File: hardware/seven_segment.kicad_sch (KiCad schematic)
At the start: 50 parts, among them J1 Conn_02x08_Odd_Even, J2 PJ-102AH, J3 7761, J4 7761, J5 Conn_01x02, SW1 SW_Push, SW2 SW_Push, SW3 SW_Push, SW4 SW_Push, U1 STM32F051K8Ux, U10 TPS22810DRV, U11 TPS22810DRV, U12 TPS22810DRV, U13 TPS22810DRV, U2 ULN2003A, U3 ULN2003A, U4 AP1117-33, U5 TPS22810DRV, U6 74HC238, U7 TPS22810DRV, U8 TPS22810DRV, U9 TPS22810DRV

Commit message: hardware: Start work on version 2
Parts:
- removed C4: C, Resistor_SMD:R_0603_1608Metric, symbol Device:C
- removed DISP1, DISP2, DISP3, DISP4, DISP5, DISP6, DISP7, DISP8: Conn_01x01, klauke:2025, symbol Connector_Generic:Conn_01x01
- removed J1: Conn_02x08_Odd_Even, Connector_PinHeader_2.54mm:PinHeader_2x08_P2.54mm_Horizontal, symbol Connector_Generic:Conn_02x08_Odd_Even
- removed J3, J4: 7761, 7761:KEYSTONE_7761, symbol 7761:7761
- removed J5: Conn_01x02, Connector_PinHeader_2.54mm:PinHeader_1x02_P2.54mm_Vertical, symbol Connector_Generic:Conn_01x02
- removed R7, R8: R, Resistor_SMD:R_0603_1608Metric, symbol Device:R
- removed SW4: SW_Push, pushbutton:TO_6083716_WRE, symbol Switch:SW_Push
- removed U10, U11, U12, U13, U5, U7, U8, U9: TPS22810DRV, Package_SON:WSON-6-1EP_2x2mm_P0.65mm_EP1x1.6mm, symbol Power_Management:TPS22810DRV
- removed U6: 74HC238, Package_SO:SOIC-16W_5.3x10.2mm_P1.27mm, symbol 74xx_IEEE:74HC238
- added BOOT0: BOOT0, TestPoint:TestPoint_Pad_D1.5mm, symbol Connector:TestPoint
- added J1: Conn_01x16, Connector_PinHeader_2.54mm:PinHeader_2x08_P2.54mm_Horizontal, symbol Connector_Generic:Conn_01x16
- added J3: Conn_01x04, Connector_JST:JST_EH_B4B-EH-A_1x04_P2.50mm_Vertical, symbol Connector_Generic:Conn_01x04
- added U10, U7, U8, U9: TPS22810DBVT, Package_TO_SOT_SMD:SOT-23-6, symbol TPS22810DBVT:TPS22810DBVT
- added U11: STM32F051C8Tx, Package_QFP:LQFP-48_7x7mm_P0.5mm, symbol MCU_ST_STM32F0:STM32F051C8Tx
- added U12: STM32F051C8Ux, Package_DFN_QFN:QFN-48-1EP_7x7mm_P0.5mm_EP5.6x5.6mm, symbol MCU_ST_STM32F0:STM32F051C8Ux
- added U5, U6: 74HC595, Package_SO:SOP-16_4.55x10.3mm_P1.27mm, symbol 74xx:74HC595
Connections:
- net sel_en is gone; now on net SWCLK: U1.25 (PA15)
- net +12V: now also U10.1 (VIN), U7.1 (VIN), U8.1 (VIN), U9.1 (VIN)
- net +3V3: now also U5.10 (~{SRCLR}), U5.16 (VCC), U6.10 (~{SRCLR}), U6.16 (VCC); no longer R9.2
- net GND: now also R9.1, U10.2 (GND), U5.8 (GND), U6.8 (GND), U7.2 (GND), U8.2 (GND), U9.2 (GND)
- net SWCLK: now also SWD1.3 (Pin_3); no longer SWD1.4 (Pin_4), U1.24 (PA14)
- net SWDIO: now also SWD1.4 (Pin_4), U1.24 (PA14); no longer SWD1.3 (Pin_3), U1.23 (PA13)
- net at U3.10 (O7): now also J1.16 (Pin_16)
- net at U3.11 (O6): now also J1.15 (Pin_15)
- net at U3.12 (O5): now also J1.14 (Pin_14)
- net at U3.13 (O4): now also J1.13 (Pin_13)
- net at U3.14 (O3): now also J1.12 (Pin_12)
- net at U3.15 (O2): now also J1.11 (Pin_11)
- net at U3.16 (O1): now also J1.10 (Pin_10)
- net at U2.10 (O7): now also J1.9 (Pin_9)
- net at U2.11 (O6): now also J1.8 (Pin_8)
- net at U2.12 (O5): now also J1.7 (Pin_7)
- net at U2.13 (O4): now also J1.6 (Pin_6)
- net at U2.14 (O3): now also J1.5 (Pin_5)
- net at U2.15 (O2): now also J1.4 (Pin_4)
- net at U2.16 (O1): now also J1.3 (Pin_3)
- net at U1.31 (BOOT0): now also R9.2, BOOT0.1; no longer R9.1
- net clrA: no longer names the net of U3.7 (I7)
- net clrA: now also U6.7 (QH); no longer U1.13 (PA7)
- net clrB: no longer names the net of U3.6 (I6)
- net clrB: now also U6.6 (QG); no longer U1.14 (PB0)
- net clrC: no longer names the net of U3.5 (I5)
- net clrC: now also U6.5 (QF); no longer U1.15 (PB1)
- net clrD: no longer names the net of U3.4 (I4)
- net clrD: now also U6.4 (QE); no longer U1.16 (PB2)
- net clrE: no longer names the net of U1.18 (PA8)
- net clrE: now also U5.13 (~{OE}), U6.13 (~{OE}); no longer U3.3 (I3)
- net clrF: no longer names the net of U3.2 (I2)
- net clrF: now also U6.2 (QC); no longer U1.21 (PA11)
- net clrG: no longer names the net of U3.1 (I1)
- net clrG: now also U6.1 (QB); no longer U1.22 (PA12)
- net sel0: no longer names the net of U1.28 (PB5)
- net sel1: no longer names the net of U1.27 (PB4)
- net sel2: no longer names the net of U1.26 (PB3)
- net setA: no longer names the net of U1.6 (PA0)
- net setA: now also U7.3 (EN/UVLO); no longer U2.7 (I7)
- net setB: no longer names the net of U1.7 (PA1)
- net setB: now also U8.3 (EN/UVLO); no longer U2.6 (I6)
- net setC: no longer names the net of U2.5 (I5)
- net setC: now also U5.5 (QF); no longer U1.8 (PA2)
- net setD: no longer names the net of U1.9 (PA3)
- net setD: now also U10.3 (EN/UVLO); no longer U2.4 (I4)
- net setE: no longer names the net of U2.3 (I3)
- net setE: now also U5.3 (QD); no longer U1.10 (PA4)
- net setF: no longer names the net of U2.2 (I2)
- net setF: now also U5.2 (QC); no longer U1.11 (PA5)
- net setG: no longer names the net of U2.1 (I1)
- net setG: now also U5.1 (QB); no longer U1.12 (PA6)
- new net: J3.2 (Pin_2), U8.6 (VOUT)
- new net: J3.4 (Pin_4), U10.6 (VOUT)
- new net: J3.1 (Pin_1), U7.6 (VOUT)
- new net: U2.4 (I4), U5.4 (QE)
- new net: U2.6 (I6), U5.6 (QG)
- new net: U2.7 (I7), U5.7 (QH)
- new net: U5.9 (QH'), U6.14 (SER)
- new net: J3.3 (Pin_3), U9.6 (VOUT)
- new net: U3.3 (I3), U6.3 (QD)
- new net: U1.8 (PA2), U9.3 (EN/UVLO)
- new net MISO: U1.12 (PA6)
- new net MOSI: U1.13 (PA7), U5.14 (SER)
- new net SCK: U1.11 (PA5), U5.11 (SRCLK), U5.12 (RCLK), U6.11 (SRCLK), U6.12 (RCLK)
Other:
- moved on the sheet: R9, SWD1, U1, U2, U3, UART1

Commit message: hardware: Version 2
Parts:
- removed C3: C, Resistor_SMD:R_0603_1608Metric, symbol Device:C
- removed SW3: SW_Push, pushbutton:TO_6083716_WRE, symbol Switch:SW_Push
- removed U11: STM32F051C8Tx, Package_QFP:LQFP-48_7x7mm_P0.5mm, symbol MCU_ST_STM32F0:STM32F051C8Tx
- removed U12: STM32F051C8Ux, Package_DFN_QFN:QFN-48-1EP_7x7mm_P0.5mm_EP5.6x5.6mm, symbol MCU_ST_STM32F0:STM32F051C8Ux
- added BT1: Battery_Cell, Battery:BatteryHolder_Keystone_3000_1x12mm, symbol Device:Battery_Cell
- added C10, C4: C, Resistor_SMD:R_0402_1005Metric_Pad0.72x0.64mm_HandSolder, symbol Device:C
- added D1: LED, Connector_PinHeader_2.54mm:PinHeader_1x02_P2.54mm_Vertical, symbol Device:LED
- added R7: 10k, Resistor_SMD:R_0603_1608Metric, symbol Device:R
- added U11: MCP7940N-xSN, Package_SO:SO-8_3.9x4.9mm_P1.27mm, symbol Timer_RTC:MCP7940N-xSN
- added Y1: Crystal, Crystal:Crystal_SMD_3215-2Pin_3.2x1.5mm, symbol Device:Crystal
- C5, C6: footprint Capacitor_THT:CP_Radial_D7.5mm_P2.50mm -> Capacitor_SMD:CP_Elec_6.3x5.9
- R3, R6, R9: value R -> 10k
- renumbered SW1 to RST1
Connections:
- net +3V3: now also R6.2, D1.2 (A), U11.8 (VCC)
- net GND: now also BT1.2 (-), C10.2, C4.2, U11.4 (VSS)
- net at U8.3 (EN/UVLO): now also U1.15 (PB1); no longer U1.7 (PA1)
- net SDA: now reaches R3.1
- net SDA: now also U1.30 (PB7), U11.5 (SDA); no longer R6.2
- net at U10.3 (EN/UVLO): now also U1.18 (PA8); no longer U1.9 (PA3)
- net at U7.3 (EN/UVLO): now also U1.14 (PB0); no longer U1.6 (PA0)
- net at U5.13 (~{OE}), U6.13 (~{OE}): now also U1.10 (PA4); no longer U1.18 (PA8)
- net at R5.1: now also U1.8 (PA2); no longer U1.29 (PB6)
- net at U9.3 (EN/UVLO): now also U1.16 (PB2); no longer U1.8 (PA2)
- net SCL: now reaches R6.1
- net SCL: now also U1.29 (PB6), U11.6 (SCL); no longer U1.30 (PB7)
- net at U1.28 (PB5): now also U11.7 (MFP)
- new net: C10.1, U11.1 (X1), Y1.2
- new net: C4.1, U11.2 (X2), Y1.1
- new net: BT1.1 (+), U11.3 (VBAT)
- new net: D1.1 (K), R7.2
- new net: R7.1, U1.9 (PA3)
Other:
- moved on the sheet: BOOT0, C1, C2, J3, R1, R2, R4, R5, R9, RST1, SW2, U10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

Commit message: hardware: revision 3
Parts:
- removed BOOT0: BOOT0, TestPoint:TestPoint_Pad_D1.5mm, symbol Connector:TestPoint
- removed BT1: Battery_Cell, Battery:BatteryHolder_Keystone_3000_1x12mm, symbol Device:Battery_Cell
- removed C10: C, Resistor_SMD:R_0402_1005Metric_Pad0.72x0.64mm_HandSolder, symbol Device:C
- removed C5, C6: C_Polarized, Capacitor_SMD:CP_Elec_6.3x5.9, symbol Device:C_Polarized
- removed D1: LED, Connector_PinHeader_2.54mm:PinHeader_1x02_P2.54mm_Vertical, symbol Device:LED
- removed SWD1, UART1: Conn_01x04, Connector_PinHeader_2.54mm:PinHeader_1x04_P2.54mm_Vertical, symbol Connector_Generic:Conn_01x04
- removed U1: STM32F051K8Ux, Package_DFN_QFN:QFN-32-1EP_5x5mm_P0.5mm_EP3.45x3.45mm, symbol MCU_ST_STM32F0:STM32F051K8Ux
- removed U10, U7, U8, U9: TPS22810DBVT, Package_TO_SOT_SMD:SOT-23-6, symbol TPS22810DBVT:TPS22810DBVT
- removed U11: MCP7940N-xSN, Package_SO:SO-8_3.9x4.9mm_P1.27mm, symbol Timer_RTC:MCP7940N-xSN
- removed U4: AP1117-33, Package_TO_SOT_SMD:SOT-223-3_TabPin2, symbol Regulator_Linear:AP1117-33
- removed Y1: Crystal, Crystal:Crystal_SMD_3215-2Pin_3.2x1.5mm, symbol Device:Crystal
- added C3: 10p, Resistor_SMD:R_0603_1608Metric, symbol Device:C
- added J5: Conn_01x06, Connector:Tag-Connect_TC2030-IDC-NL_2x03_P1.27mm_Vertical, symbol Connector_Generic:Conn_01x06
- added K1, K2, K3, K4: ~, 00_customfootprints:G6DN-1A-SL, symbol 00_customsymbols:Relay
- added L1: 2.2u, Inductor_SMD:L_Vishay_IHLP-1212, symbol Device:L
- added R10, R11: 10k, Resistor_SMD:R_0603_1608Metric, symbol Device:R
- added R8: R, Resistor_SMD:R_0603_1608Metric, symbol Device:R
- added U1: ESP32-WROOM-32E, RF_Module:ESP32-WROOM-32D, symbol RF_Module:ESP32-WROOM-32E
- added U4: TPS562200, Package_TO_SOT_SMD:SOT-23-6, symbol Regulator_Switching:TPS562200
- added U7: ULN2003A, Package_SO:SOP-16_3.9x9.9mm_P1.27mm, symbol Transistor_Array:ULN2003A
- C4: value C -> 0.1u; footprint Resistor_SMD:R_0402_1005Metric_Pad0.72x0.64mm_HandSolder -> Resistor_SMD:R_0603_1608Metric
- C7, C8: value C -> 22u; footprint Resistor_SMD:R_0805_2012Metric -> Capacitor_SMD:C_0805_2012Metric
- C9: value C -> 10u; footprint Resistor_SMD:R_0805_2012Metric -> Capacitor_SMD:C_0805_2012Metric
- J1: footprint Connector_PinHeader_2.54mm:PinHeader_2x08_P2.54mm_Horizontal -> Connector_PinHeader_2.54mm:PinHeader_2x08_P2.54mm_Vertical
- R1, R2: value R -> 10k
- R3, R6, R7: value 10k -> R
- R9: value 10k -> 33.2k
- U2, U3, U5, U6: footprint Package_SO:SOP-16_4.55x10.3mm_P1.27mm -> Package_SO:SOP-16_3.9x9.9mm_P1.27mm
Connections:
- net +12V: now also C9.1, R3.2, R6.2, R7.2, K1.3, K2.3, K3.3, K4.3, R11.1, R8.2, U4.3 (VIN), U7.9 (COM)
- net +3V3: now also R1.1, R2.1, R9.1, J5.2 (Pin_2), L1.2, U1.2 (VDD); no longer C9.1, R1.2, R2.2, R3.2, R6.2
- net GND: now also C3.2, J5.4 (Pin_4), R10.2, U1.1 (GND), U1.15 (GND), U1.38 (GND), U1.39 (GND), U4.1 (GND), U7.5 (I5), U7.6 (I6), U7.7 (I7), U7.8 (GND); no longer C4.2, R9.1
- net at C4.1: now also U4.6 (VBST)
- net at J3.2 (Pin_2): now also K2.4
- net at R9.2: now also R10.1, U4.4 (VFB)
- net at J3.4 (Pin_4): now also K4.4
- net at R4.1: now also C1.1, U1.31 (IO19)
- net at R4.2, RST1.1: no longer C1.1, R1.1
- net at J3.1 (Pin_1): now also K1.4
- net at U5.1 (QB): now also U2.7 (I7); no longer U2.1 (I1)
- net at U5.13 (~{OE}), U6.13 (~{OE}): now also U1.9 (IO33)
- net at U5.2 (QC): now also U2.6 (I6); no longer U2.2 (I2)
- net at U5.3 (QD): now also U2.5 (I5); no longer U2.3 (I3)
- net at U5.5 (QF): now also U2.3 (I3); no longer U2.5 (I5)
- net at U5.6 (QG): now also U2.2 (I2); no longer U2.6 (I6)
- net at U5.7 (QH): now also U2.1 (I1); no longer U2.7 (I7)
- net at J3.3 (Pin_3): now also K3.4
- net at U6.1 (QB): now also U3.7 (I7); no longer U3.1 (I1)
- net at U6.2 (QC): now also U3.6 (I6); no longer U3.2 (I2)
- net at U6.3 (QD): now also U3.5 (I5); no longer U3.3 (I3)
- net at U6.5 (QF): now also U3.3 (I3); no longer U3.5 (I5)
- net at U6.6 (QG): now also U3.2 (I2); no longer U3.6 (I6)
- net at U6.7 (QH): now also U3.1 (I1); no longer U3.7 (I7)
- net at J1.10 (Pin_10): now also U3.10 (O7); no longer U3.16 (O1)
- net at J1.11 (Pin_11): now also U3.11 (O6); no longer U3.15 (O2)
- net at J1.12 (Pin_12): now also U3.12 (O5); no longer U3.14 (O3)
- net at J1.14 (Pin_14): now also U3.14 (O3); no longer U3.12 (O5)
- net at J1.15 (Pin_15): now also U3.15 (O2); no longer U3.11 (O6)
- net at J1.16 (Pin_16): now also U3.16 (O1); no longer U3.10 (O7)
- net at J1.3 (Pin_3): now also U2.10 (O7); no longer U2.16 (O1)
- net at J1.4 (Pin_4): now also U2.11 (O6); no longer U2.15 (O2)
- net at J1.5 (Pin_5): now also U2.12 (O5); no longer U2.14 (O3)
- net at J1.7 (Pin_7): now also U2.14 (O3); no longer U2.12 (O5)
- net at J1.8 (Pin_8): now also U2.15 (O2); no longer U2.11 (O6)
- net at J1.9 (Pin_9): now also U2.16 (O1); no longer U2.10 (O7)
- net at R5.1: now also C2.1, U1.26 (IO4)
- net at R5.2, SW2.1: no longer C2.1, R2.1
- net at R7.1: now also K3.2
- net MOSI: no longer names the net of U5.14 (SER)
- net MOSI: now also U1.8 (IO32)
- net SCK: no longer names the net of U5.11 (SRCLK), U5.12 (RCLK), U6.11 (SRCLK), U6.12 (RCLK)
- net SCK: now also U1.10 (IO25)
- net SCL: no longer names the net of R6.1
- net SCL: now also K2.2
- net SDA: no longer names the net of R3.1
- net SDA: now also K1.2
- new net: K1.1, U7.15 (O2)
- new net: R11.2, U4.5 (EN)
- new net: C3.1, J5.1 (Pin_1), R2.2, U1.3 (EN)
- new net: J5.3 (Pin_3), U1.34 (RXD0/IO3)
- new net: J5.5 (Pin_5), U1.35 (TXD0/IO1)
- new net: J5.6 (Pin_6), U1.25 (IO0)
- new net: K3.1, U7.13 (O4)
- new net: R1.2, U1.27 (IO16)
- new net: C4.2, L1.1, U4.2 (SW)
- new net: K4.1, U7.14 (O3)
- new net: K4.2, R8.1
- new net: K2.1, U7.16 (O1)
- new net: U1.28 (IO17), U7.1 (I1)
- new net: U1.30 (IO18), U7.2 (I2)
- new net: U1.36 (IO22), U7.3 (I3)
- new net: U1.37 (IO23), U7.4 (I4)
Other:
- moved on the sheet: J2, J3, R4, R5, RST1, SW2

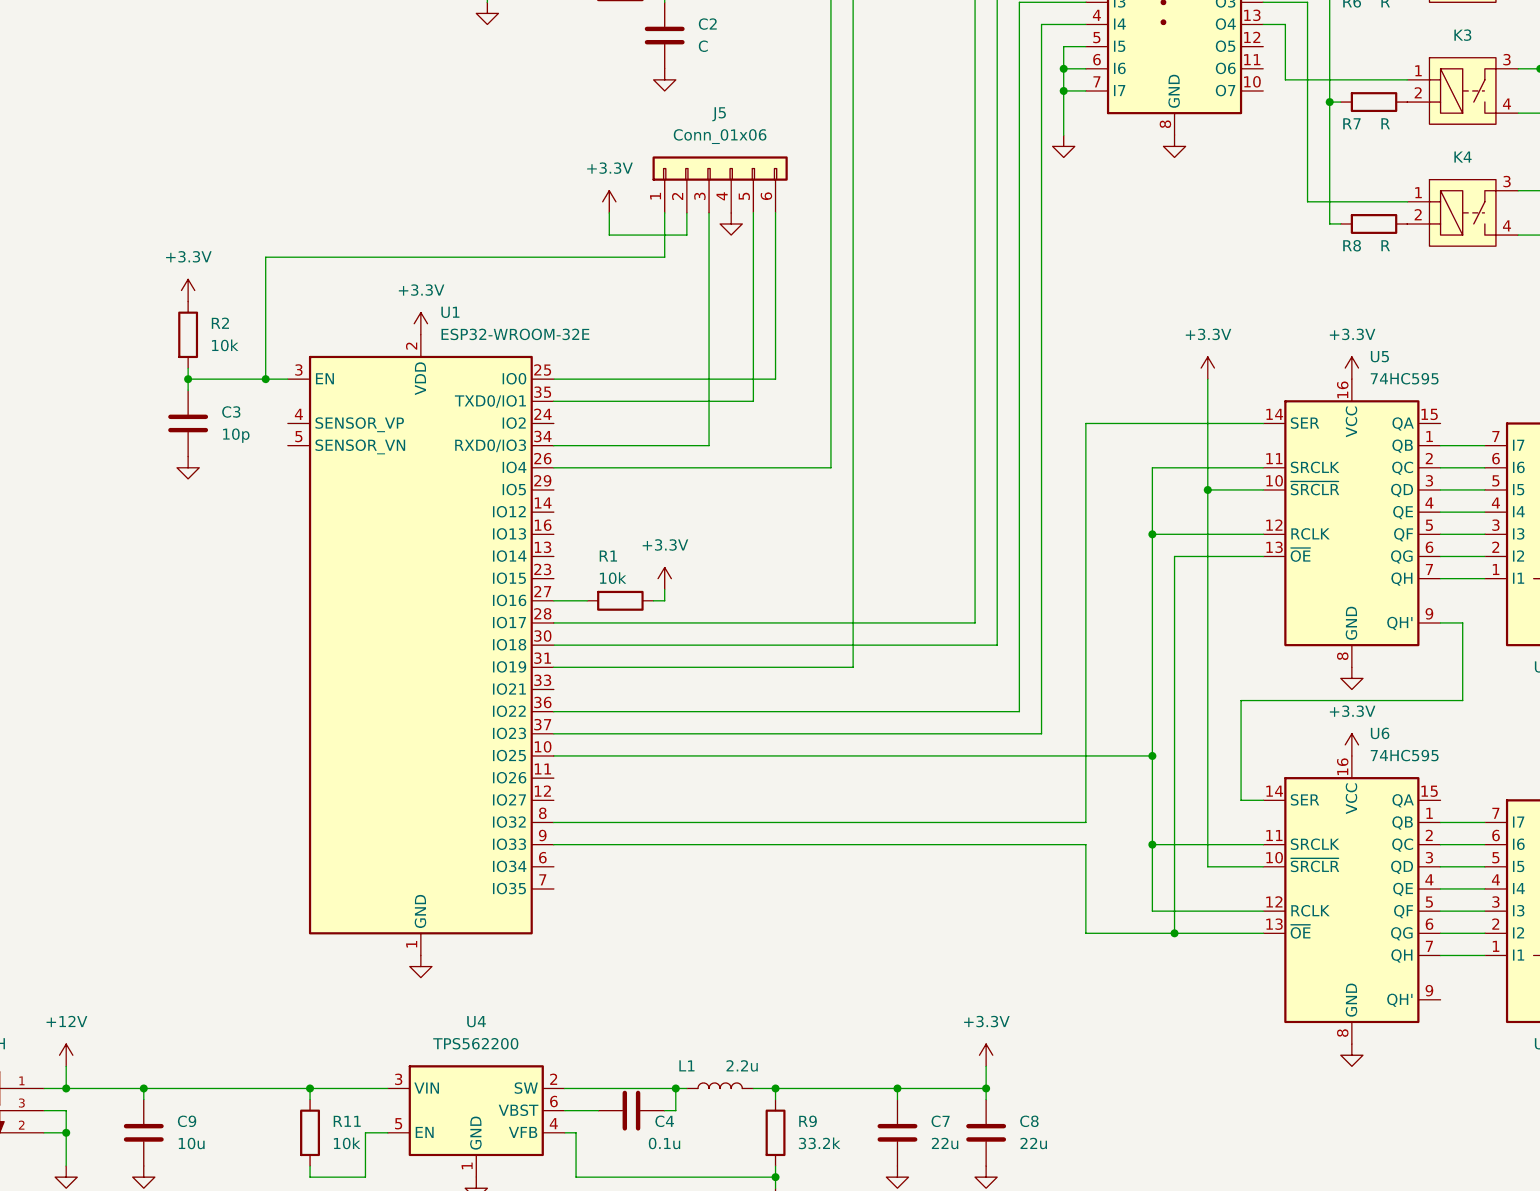
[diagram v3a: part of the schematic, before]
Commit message: hardware: migrate to kicad 8
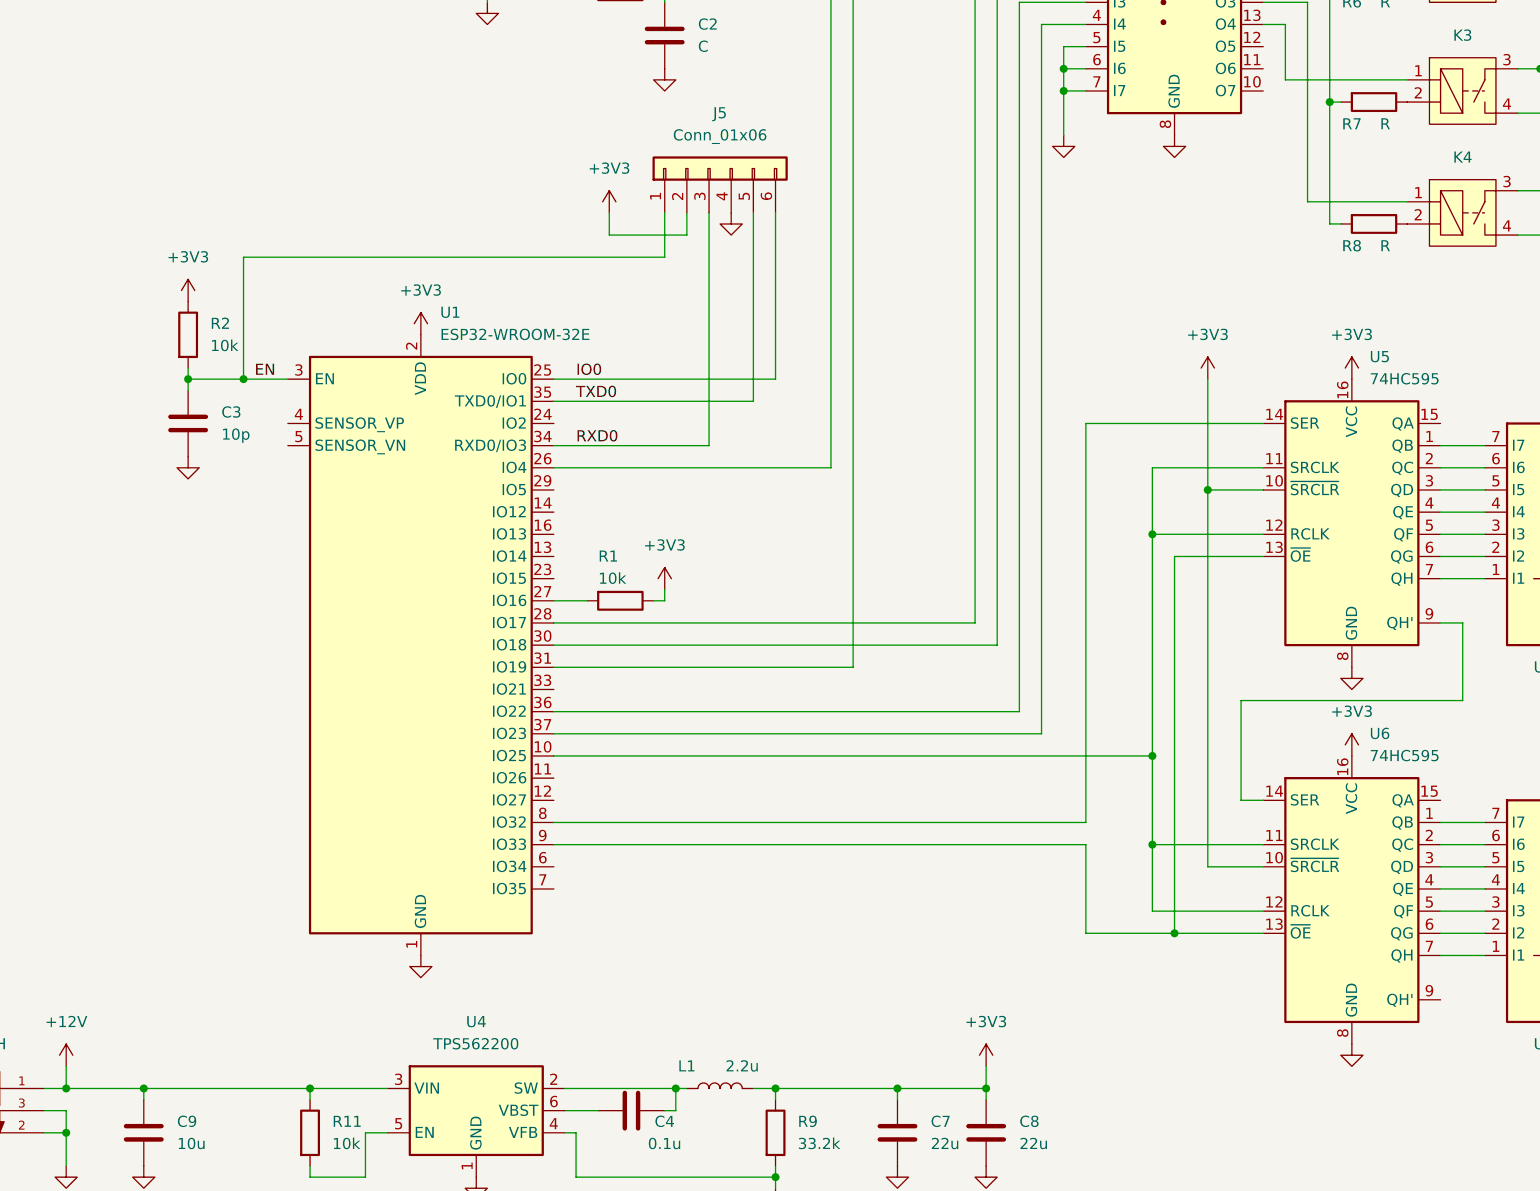
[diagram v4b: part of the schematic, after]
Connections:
- net EN: now reaches C3.1, J5.1 (Pin_1), R2.2, U1.3 (EN)
- net RXD0: now reaches J5.3 (Pin_3), U1.34 (RXD0/IO3)
- net TXD0: now reaches J5.5 (Pin_5), U1.35 (TXD0/IO1)
- net IO0: now reaches J5.6 (Pin_6), U1.25 (IO0)
